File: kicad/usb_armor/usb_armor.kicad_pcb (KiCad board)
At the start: 2 copper layers, 2 parts

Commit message: initial placement completed
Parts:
- added C1: 10n, SquantorRcl:C_0805, F.Cu at (160.2, 92.6)
- added C2: 2.2u, SquantorRcl:C_0805, F.Cu at (143.3, 92.6)
- added D1: 5V_TVS, Diode_SMD:D_SMC, F.Cu at (153.7, 87.1)
- added D2: LED, LED_THT:LED_D3.0mm, F.Cu at (149.1, 78.8)
- added J1: USB-ID, SquantorUsb:USB-muB-SMD_TH, F.Cu at (159.9, 86.8)
- added J2: USB, SquantorUsb:USB-A-TH, F.Cu at (137.3, 86.8)
- added R1: R, SquantorRcl:R_0603_hand, F.Cu at (156.9, 80.3)
- added R10: TBD, SquantorRcl:R_0603_hand, F.Cu at (142.3, 83.7)
- added R11: TBD, SquantorRcl:R_0603_hand, F.Cu at (142.3, 90.0)
- added R12: TBD, SquantorRcl:R_0603_hand, F.Cu at (143.9, 83.7)
- added R13: TBD, SquantorRcl:R_0603_hand, F.Cu at (143.9, 90.0)
- added R2: R, SquantorRcl:R_0603_hand, F.Cu at (155.3, 80.3)
- added R3: TBD, SquantorRcl:R_0603_hand, F.Cu at (147.8, 83.7)
- added R4: TBD, SquantorRcl:R_0603_hand, F.Cu at (147.8, 90.0)
- added R5: 1K, SquantorRcl:R_0603_hand, F.Cu at (143.0, 80.7)
- added R6: TBD, SquantorRcl:R_0603_hand, F.Cu at (149.4, 83.7)
- added R7: TBD, SquantorRcl:R_0603_hand, F.Cu at (149.4, 90.0)
- added R8: 0, SquantorRcl:R_0603_hand, F.Cu at (145.8, 86.0)
- added R9: 0, SquantorRcl:R_0603_hand, F.Cu at (145.8, 87.7)
- N2: value 20181108 -> 20190119

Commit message: further layout
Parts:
- moved D1 16.1 mm to (137.6, 88.3)
- moved C2 12.3 mm to (146.2, 80.6), turned to 180 degrees
- moved D2 9.17 mm to (140.2, 81.0)
- moved R5 7.61 mm to (135.4, 81.1), turned to 270 degrees
- moved C1 7.21 mm to (153.0, 92.3)
- moved J2 6.96 mm to (130.4, 85.9)
- moved J1 6.70 mm to (153.2, 86.8)
- moved R1 4.42 mm to (152.5, 80.7)
- moved R2 4.42 mm to (150.9, 80.7)
- moved R3 0.10 mm to (147.7, 83.7)
- moved R4 0.10 mm to (147.7, 90.0)
- moved R12 0.10 mm to (144.0, 83.7)
- moved R13 0.10 mm to (144.0, 90.0)
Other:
- board outline added: 28 x 18 mm
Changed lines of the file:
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@@
   (general
     (thickness 1.6)
-    (drawings 0)
+    (drawings 4)
     (tracks 0)
     (zones 0)
@@
   )
   (module SquantorRcl:C_0805 (layer F.Cu)
-    (at 160.2 92.6)
+    (at 153 92.3)
     (descr "Capacitor SMD 0805, reflow soldering, AVX (see smccp.pdf)")
     (tags "capacitor 0805")
@@
   )
   (module SquantorRcl:C_0805 (layer F.Cu)
-    (at 143.3 92.6)
+    (at 146.2 80.6 180)
     (descr "Capacitor SMD 0805, reflow soldering, AVX (see smccp.pdf)")
     (tags "capacitor 0805")
     (attr smd)
-    (fp_text reference C2 (at 0 -2.1) (layer F.SilkS)
-      (effects (font (size 1 1) (thickness 0.15)))
-    )
-    (fp_text value 2.2u (at 0 2.1) (layer F.Fab)
+    (fp_text reference C2 (at 0 -2.1 180) (layer F.SilkS)
+      (effects (font (size 1 1) (thickness 0.15)))
+    )
+    (fp_text value 2.2u (at 0 2.1 180) (layer F.Fab)
       (effects (font (size 1 1) (thickness 0.15)))
     )
@@
     (fp_line (start 1 0.625) (end -1 0.625) (layer F.Fab) (width 0.15))
     (fp_line (start -1 0.625) (end -1 -0.625) (layer F.Fab) (width 0.15))
-    (pad 2 smd rect (at 1 0) (size 1 1.25) (layers F.Cu F.Paste F.Mask)
-      (net 3 VCC))
-    (pad 1 smd rect (at -1 0) (size 1 1.25) (layers F.Cu F.Paste F.Mask)
+    (pad 2 smd rect (at 1 0 180) (size 1 1.25) (layers F.Cu F.Paste F.Mask)
+      (net 3 VCC))
+    (pad 1 smd rect (at -1 0 180) (size 1 1.25) (layers F.Cu F.Paste F.Mask)
       (net 1 GND))
     (model Capacitors_SMD.3dshapes/C_0805.wrl
@@
   )
   (module Diode_SMD:D_SMC (layer F.Cu)
-    (at 153.7 87.1 270)
+    (at 137.6 88.3 270)
     (descr "Diode SMC (DO-214AB)")
     (tags "Diode SMC (DO-214AB)")
@@
   )
   (module LED_THT:LED_D3.0mm (layer F.Cu)
-    (at 149.1 78.8 180)
+    (at 140.2 81 180)
     (descr "LED, diameter 3.0mm, 2 pins")
     (tags "LED diameter 3.0mm 2 pins")
@@
   )
   (module SquantorUsb:USB-muB-SMD_TH (layer F.Cu)
-    (at 159.9 86.8 90)
+    (at 153.2 86.8 90)
     (fp_text reference J1 (at 0 -3 90) (layer F.SilkS)
       (effects (font (size 1 1) (thickness 0.15)))
@@
   )
   (module SquantorUsb:USB-A-TH (layer F.Cu)
-    (at 137.3 86.8)
+    (at 130.4 85.9)
     (descr "USB SERIES A HOLE MOUNTED")
     (tags "USB SERIES A HOLE MOUNTED")
@@
   )
   (module SquantorRcl:R_0603_hand (layer F.Cu)
-    (at 156.9 80.3 90)
+    (at 152.5 80.7 90)
     (descr "Resistor SMD 0603, reflow soldering, Vishay (see dcrcw.pdf)")
     (tags "resistor 0603")
@@
   )
   (module SquantorRcl:R_0603_hand (layer F.Cu)
-    (at 155.3 80.3 90)
+    (at 150.9 80.7 90)
     (descr "Resistor SMD 0603, reflow soldering, Vishay (see dcrcw.pdf)")
     (tags "resistor 0603")
@@
   )
   (module SquantorRcl:R_0603_hand (layer F.Cu)
-    (at 147.8 83.7 90)
+    (at 147.7 83.7 90)
     (descr "Resistor SMD 0603, reflow soldering, Vishay (see dcrcw.pdf)")
     (tags "resistor 0603")
@@
   )
   (module SquantorRcl:R_0603_hand (layer F.Cu)
-    (at 147.8 90 90)
+    (at 147.7 90 90)
     (descr "Resistor SMD 0603, reflow soldering, Vishay (see dcrcw.pdf)")
     (tags "resistor 0603")
@@
   )
   (module SquantorRcl:R_0603_hand (layer F.Cu)
-    (at 143 80.7 180)
-    (descr "Resistor SMD 0603, reflow soldering, Vishay (see dcrcw.pdf)")
-    (tags "resistor 0603")
-    (attr smd)
-    (fp_text reference R5 (at 0 -1.9 180) (layer F.SilkS)
-      (effects (font (size 1 1) (thickness 0.15)))
-    )
-    (fp_text value 1K (at 0 1.9 180) (layer F.Fab)
-      (effects (font (size 1 1) (thickness 0.15)))
-    )
-    (fp_line (start -0.5 -0.675) (end 0.5 -0.675) (layer F.SilkS) (width 0.15))
-    (fp_line (start 0.5 0.675) (end -0.5 0.675) (layer F.SilkS) (width 0.15))
-    (fp_line (start 1.5 -0.8) (end 1.5 0.8) (layer F.CrtYd) (width 0.05))
-    (fp_line (start -1.5 -0.8) (end -1.5 0.8) (layer F.CrtYd) (width 0.05))
-    (fp_line (start -1.5 0.8) (end 1.5 0.8) (layer F.CrtYd) (width 0.05))
-    (fp_line (start -1.5 -0.8) (end 1.5 -0.8) (layer F.CrtYd) (width 0.05))
-    (fp_line (start -0.8 -0.4) (end 0.8 -0.4) (layer F.Fab) (width 0.1))
-    (fp_line (start 0.8 -0.4) (end 0.8 0.4) (layer F.Fab) (width 0.1))
-    (fp_line (start 0.8 0.4) (end -0.8 0.4) (layer F.Fab) (width 0.1))
-    (fp_line (start -0.8 0.4) (end -0.8 -0.4) (layer F.Fab) (width 0.1))
-    (pad 2 smd rect (at 0.85 0 180) (size 0.7 0.9) (layers F.Cu F.Paste F.Mask)
-      (net 3 VCC))
-    (pad 1 smd rect (at -0.85 0 180) (size 0.7 0.9) (layers F.Cu F.Paste F.Mask)
+    (at 135.4 81.1 270)
+    (descr "Resistor SMD 0603, reflow soldering, Vishay (see dcrcw.pdf)")
+    (tags "resistor 0603")
+    (attr smd)
+    (fp_text reference R5 (at 0 -1.9 270) (layer F.SilkS)
+      (effects (font (size 1 1) (thickness 0.15)))
+    )
+    (fp_text value 1K (at 0 1.9 270) (layer F.Fab)
+      (effects (font (size 1 1) (thickness 0.15)))
+    )
+    (fp_line (start -0.5 -0.675) (end 0.5 -0.675) (layer F.SilkS) (width 0.15))
+    (fp_line (start 0.5 0.675) (end -0.5 0.675) (layer F.SilkS) (width 0.15))
+    (fp_line (start 1.5 -0.8) (end 1.5 0.8) (layer F.CrtYd) (width 0.05))
+    (fp_line (start -1.5 -0.8) (end -1.5 0.8) (layer F.CrtYd) (width 0.05))
+    (fp_line (start -1.5 0.8) (end 1.5 0.8) (layer F.CrtYd) (width 0.05))
+    (fp_line (start -1.5 -0.8) (end 1.5 -0.8) (layer F.CrtYd) (width 0.05))
+    (fp_line (start -0.8 -0.4) (end 0.8 -0.4) (layer F.Fab) (width 0.1))
+    (fp_line (start 0.8 -0.4) (end 0.8 0.4) (layer F.Fab) (width 0.1))
+    (fp_line (start 0.8 0.4) (end -0.8 0.4) (layer F.Fab) (width 0.1))
+    (fp_line (start -0.8 0.4) (end -0.8 -0.4) (layer F.Fab) (width 0.1))
+    (pad 2 smd rect (at 0.85 0 270) (size 0.7 0.9) (layers F.Cu F.Paste F.Mask)
+      (net 3 VCC))
+    (pad 1 smd rect (at -0.85 0 270) (size 0.7 0.9) (layers F.Cu F.Paste F.Mask)
       (net 4 "Net-(D2-Pad2)"))
     (model Resistors_SMD.3dshapes/R_0603.wrl
@@
   )
   (module SquantorRcl:R_0603_hand (layer F.Cu)
-    (at 143.9 83.7 90)
+    (at 144 83.7 90)
     (descr "Resistor SMD 0603, reflow soldering, Vishay (see dcrcw.pdf)")
     (tags "resistor 0603")
@@
   )
   (module SquantorRcl:R_0603_hand (layer F.Cu)
-    (at 143.9 90 90)
+    (at 144 90 90)
     (descr "Resistor SMD 0603, reflow soldering, Vishay (see dcrcw.pdf)")
     (tags "resistor 0603")
@@
     )
   )
+  (gr_line (start 156 77) (end 128 77) (layer Edge.Cuts) (width 0.2))
+  (gr_line (start 156 95) (end 156 77) (layer Edge.Cuts) (width 0.2))
+  (gr_line (start 128 95) (end 156 95) (layer Edge.Cuts) (width 0.2))
+  (gr_line (start 128 77) (end 128 95) (layer Edge.Cuts) (width 0.2))
 )

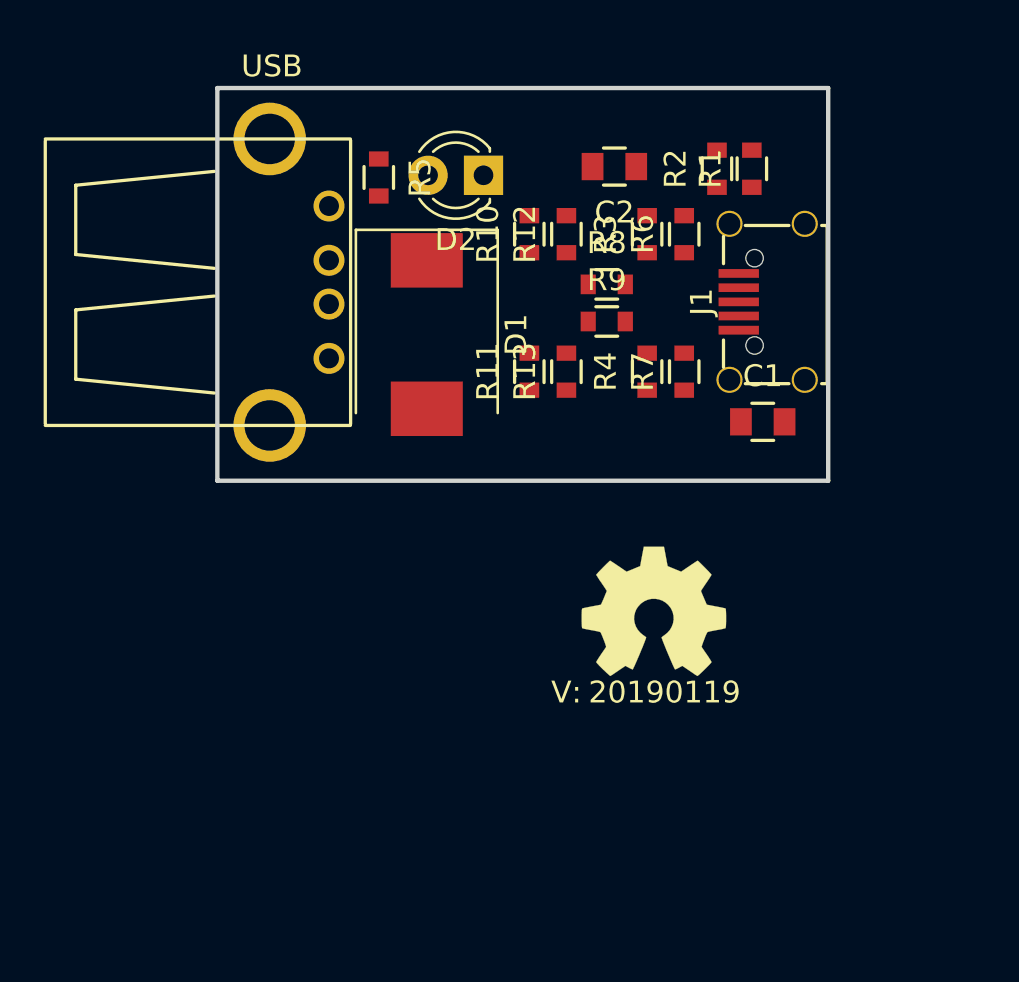
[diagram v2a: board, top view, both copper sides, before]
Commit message: some small placement optimizations
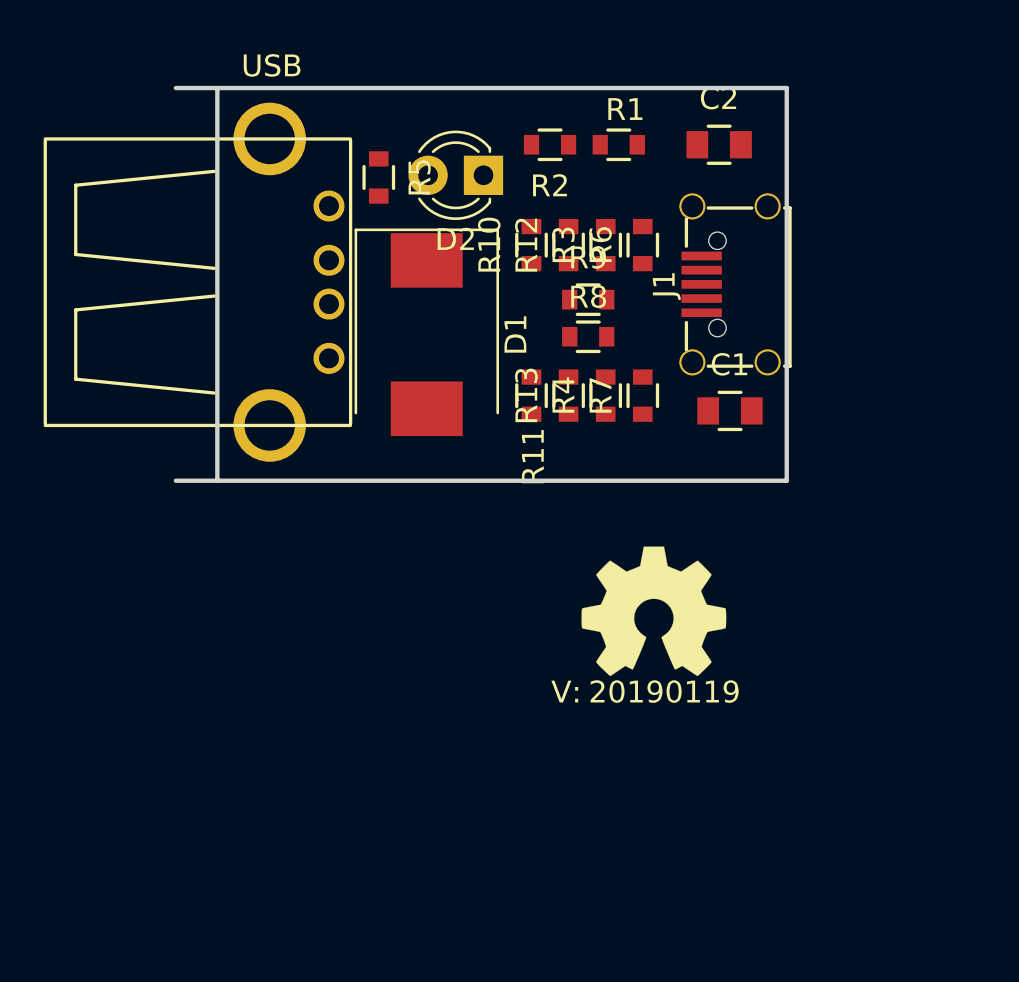
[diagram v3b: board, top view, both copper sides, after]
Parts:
- moved R2 7.73 mm to (143.2, 79.6), turned to 180 degrees
- moved R1 6.20 mm to (146.4, 79.6), turned to 0 degrees
- moved C2 4.90 mm to (151.0, 79.6), turned to 0 degrees
- moved R8 2.55 mm to (145.0, 88.4)
- moved R7 2.20 mm to (147.5, 91.1)
- moved R4 2.20 mm to (145.8, 91.1)
- moved R6 1.96 mm to (147.5, 84.2)
- moved R3 1.96 mm to (145.8, 84.2)
- moved J1 1.88 mm to (151.5, 86.0)
- moved C1 1.58 mm to (151.5, 91.8)
- moved R9 1.31 mm to (145.0, 86.7)
- moved R11 1.10 mm to (142.4, 91.1)
- moved R13 1.10 mm to (144.1, 91.1)
- moved R10 0.51 mm to (142.4, 84.2)
- moved R12 0.51 mm to (144.1, 84.2)
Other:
- outline, holes or cut-outs redrawn

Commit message: redid usb armor project with nicer box template
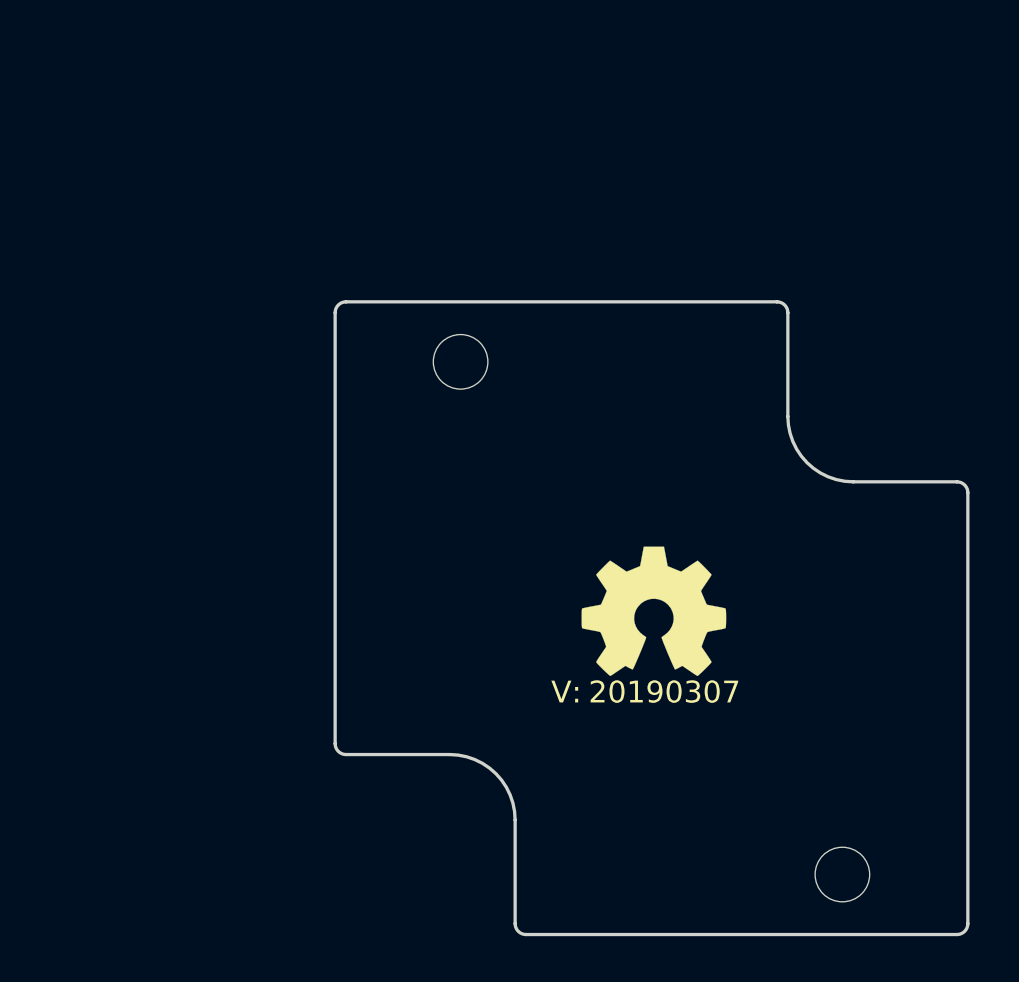
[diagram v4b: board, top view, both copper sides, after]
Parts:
- removed C1: 10n, SquantorRcl:C_0805
- removed C2: 2.2u, SquantorRcl:C_0805
- removed D1: 5V_TVS, Diode_SMD:D_SMC
- removed D2: LED, LED_THT:LED_D3.0mm
- removed J1: USB-ID, SquantorUsb:USB-muB-SMD_TH
- removed J2: USB, SquantorUsb:USB-A-TH
- removed R1, R2: R, SquantorRcl:R_0603_hand
- removed R10, R11, R12, R13, R3, R4, R6, R7: TBD, SquantorRcl:R_0603_hand
- removed R5: 1K, SquantorRcl:R_0603_hand
- removed R8, R9: 0, SquantorRcl:R_0603_hand
- added H1: Drill_Hole_no_metal, SquantorPcbOutline:MountingHole_2.5mm_no_metal, F.Cu at (139.2, 89.5)
- added H2: Drill_Hole_no_metal, SquantorPcbOutline:MountingHole_2.5mm_no_metal, F.Cu at (156.7, 113.0)
- N2: value 20190119 -> 20190307
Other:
- board size 28 x 18 mm -> 29 x 29 mm
- rule pad_to_mask_clearance: 0.2 -> 0.1
- rule solder_mask_min_width: 0.25 -> 0.15

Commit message: initial schematic, routing, silk placement
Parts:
- added J1: USB, SquantorUsb:USB_A-Plug-generic, F.Cu at (137.3, 99.5)
- added J2: USB, SquantorUsb:USB-A-TH, F.Cu at (151.9, 101.9)
- added R1: TBD, SquantorRcl:R_0603_hand, F.Cu at (143.7, 99.8)
- added R10: TBD, SquantorRcl:R_0603_hand, F.Cu at (145.7, 97.5)
- added R2: TBD, SquantorRcl:R_0603_hand, F.Cu at (143.7, 101.4)
- added R3: TBD, SquantorRcl:R_0603_hand, F.Cu at (140.1, 97.5)
- added R4: TBD, SquantorRcl:R_0603_hand, F.Cu at (140.1, 103.7)
- added R5: TBD, SquantorRcl:R_0603_hand, F.Cu at (141.7, 97.5)
- added R6: TBD, SquantorRcl:R_0603_hand, F.Cu at (141.7, 103.7)
- added R7: TBD, SquantorRcl:R_0603_hand, F.Cu at (147.3, 103.7)
- added R8: TBD, SquantorRcl:R_0603_hand, F.Cu at (147.3, 97.5)
- added R9: TBD, SquantorRcl:R_0603_hand, F.Cu at (145.7, 103.7)
- N2: value 20190307 -> 20190401
- moved N1 10.3 mm to (146.5, 111.2)
- moved N2 10.3 mm to (147.4, 115.0)
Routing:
- net /Shield: track 0.00 -> 47.2 mm
- net /IN_USB-D-: track 0.00 -> 10.5 mm, vias 0 -> 2
- net /OUT_USB-D+: track 0.00 -> 10.4 mm, vias 0 -> 2
- net /OUT_USB-D-: track 0.00 -> 10.2 mm, vias 0 -> 1
- net /IN_USB-D+: track 0.00 -> 9.54 mm, vias 0 -> 2
- net /GND: track 0.00 -> 9.48 mm
- added copper zone on B.Cu, net /GND
- added copper zone on F.Cu, net /VBUS
